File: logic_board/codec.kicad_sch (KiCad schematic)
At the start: 27 parts, among them J1 SJ3-35083C-TR, J4 Conn_01x02, U2 WM8904CGEFL/V, U6 TLV9061xDBV

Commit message: Fix DRC and ERC violations
Also updated some design rules to be consistent with fab.
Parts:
- CR3: footprint Custom_Footprints:1004DFN_LTF -> 1004DFN_LTF
- D2: footprint Diode_SMD:D_SOD-323F -> Diode_SMD:D_SOD-882
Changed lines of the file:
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@@
 			)
 		)
-		(property "Footprint" "Custom_Footprints:1004DFN_LTF"
-			(at 62.23 157.48 0)
+		(property "Footprint" "1004DFN_LTF"
+			(at 51.308 144.78 0)
 			(effects
 				(font
@@
 		)
 		(property "Datasheet" "SP1004U-ULC-04UTG"
-			(at 62.23 157.48 0)
+			(at 52.07 149.098 0)
 			(effects
 				(font
@@
 			)
 		)
-		(property "Footprint" "Diode_SMD:D_SOD-323F"
+		(property "Footprint" "Diode_SMD:D_SOD-882"
 			(at 57.15 106.68 0)
 			(effects
@@
 			)
 		)
-		(property "Datasheet" "https://jlcpcb.com/partdetail/BORN-PESD5V0L1BAN/C920305"
+		(property "Datasheet" "https://assets.nexperia.com/documents/data-sheet/PESD5V0L1UL.pdf"
 			(at 67.31 106.68 0)
 			(effects
@@
 			)
 		)
-		(property "Description" "Low capacitance unidirectional ESD protection diode, 5V, SOD-323"
+		(property "Description" "Low capacitance unidirectional ESD protection diode, 5V, SOD-882"
 			(at 69.85 106.68 0)
 			(effects

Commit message: All signals now routed.
A bit rough, needs some cleanup.
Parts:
- added C31: 0.1uF, Capacitor_SMD:C_0603_1608Metric, symbol Device:C
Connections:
- net +3V3: now also C31.1
- net GND: now also C31.2
- net at C14.2: now also U2.25 (IN1R/DMICDAT2); no longer U2.24 (IN2R)
- net at C15.2: now also U2.26 (IN2L); no longer U2.25 (IN1R/DMICDAT2)
- net at C11.2: now also U2.24 (IN2R); no longer U2.26 (IN2L)

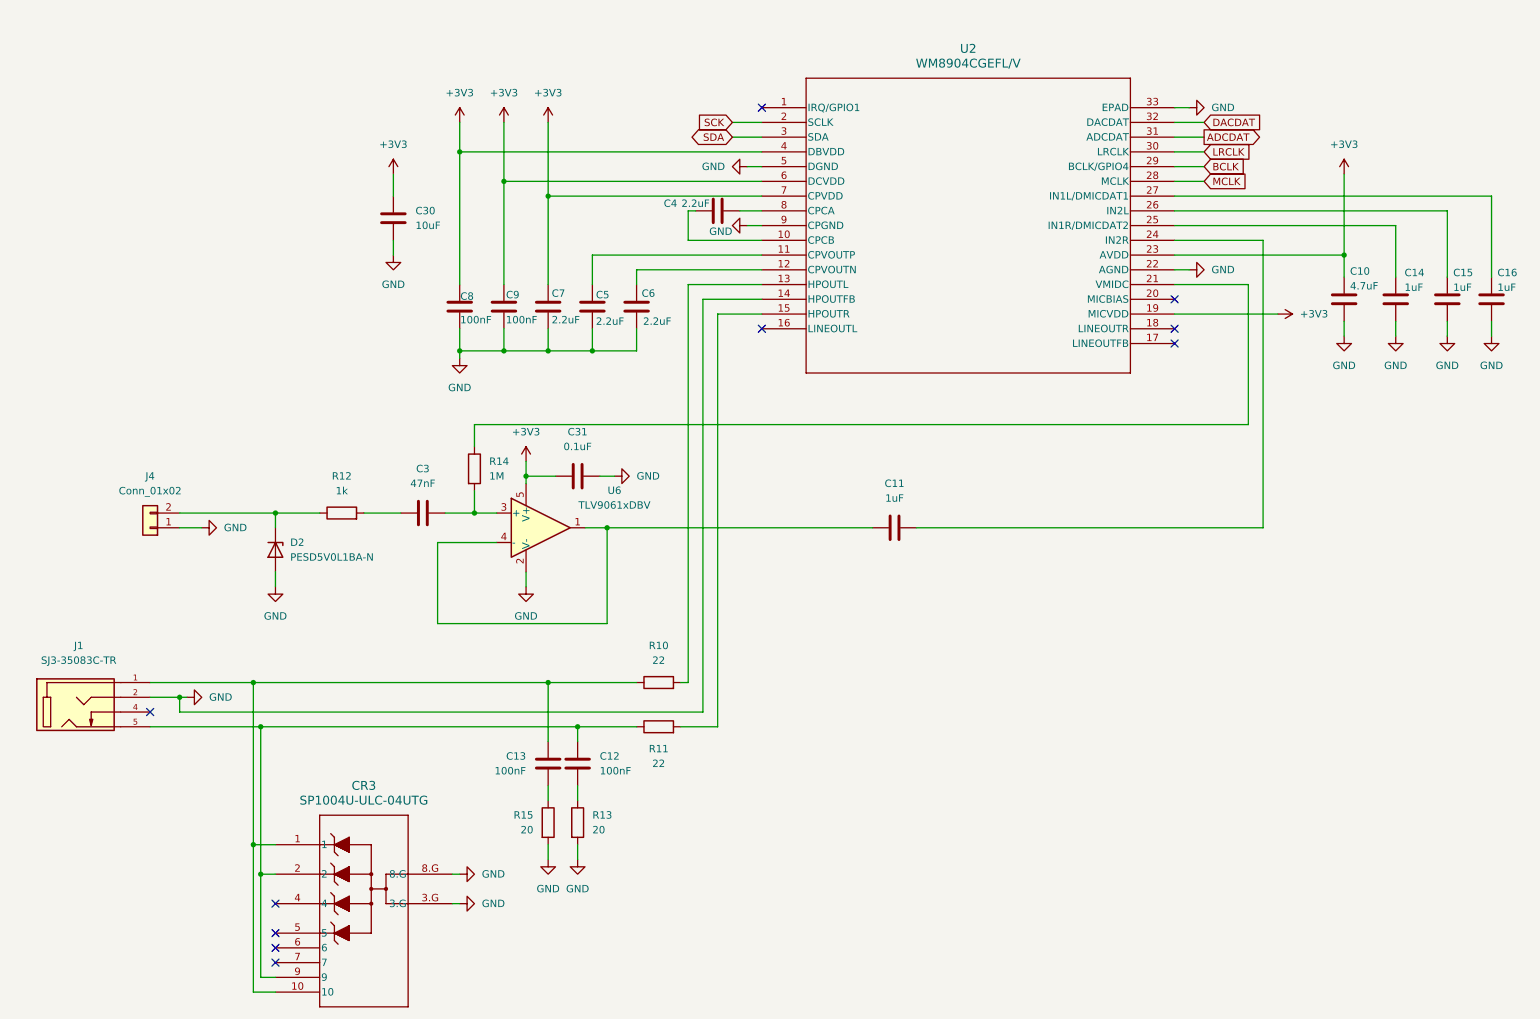
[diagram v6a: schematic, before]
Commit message: Replace WM8904 codec with ES8388
The latter is simpler. Specifically, it doesn't require a 1.8v supply (which I had neglected to hook up). It also doesn't require a ground feedback line from the headphone outputs. It also has a beefier output stage (40mW headphone output vs. 28 @ 30 ohms for the old one)
Also changed the interface from I2S to SPI, avoiding the need for pullup resistors (also missing from previous iteration).
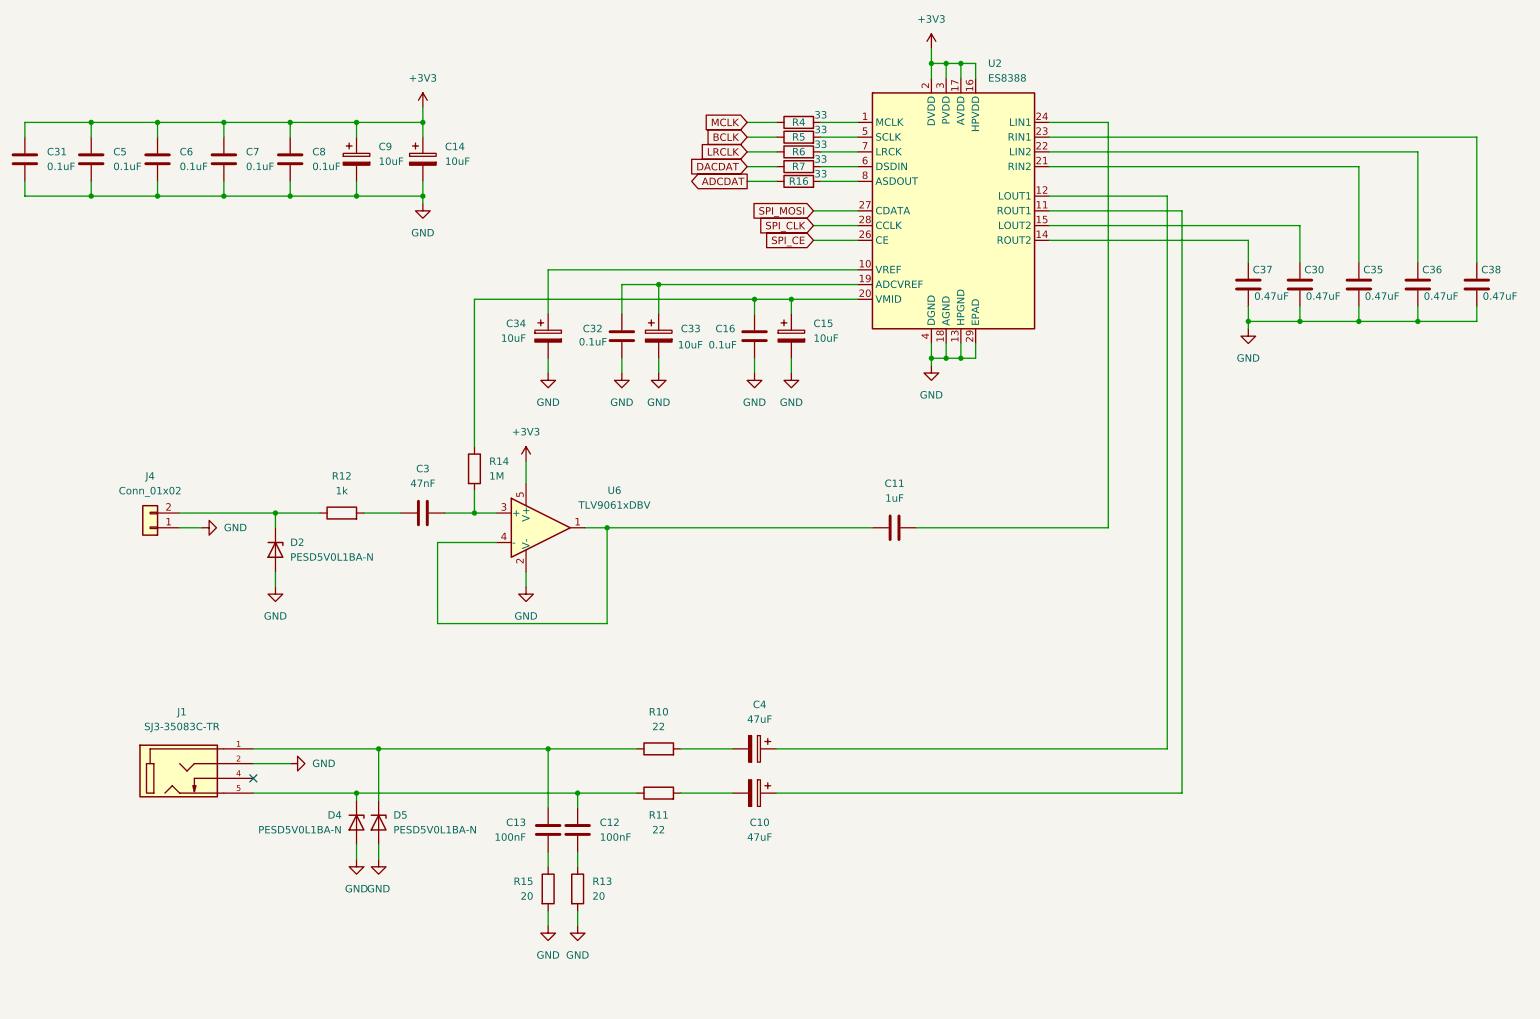
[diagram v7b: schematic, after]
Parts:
- removed C10: 4.7uF, Capacitor_SMD:C_0603_1608Metric, symbol Device:C
- removed C14, C15: 1uF, Capacitor_SMD:C_0603_1608Metric, symbol Device:C
- removed C4: 2.2uF, Capacitor_SMD:C_0603_1608Metric, symbol Device:C
- removed C9: 100nF, Capacitor_SMD:C_0603_1608Metric, symbol Device:C
- removed CR3: SP1004U-ULC-04UTG, 1004DFN_LTF, symbol Custom_Symbols:SP1004U-ULC-04UTG
- removed U2: WM8904CGEFL/V, Custom_Footprints:QFN32_4X4_CIR, symbol Custom_Symbols:WM8904CGEFL_V
- added C10, C4: 47uF, Capacitor_SMD:C_1206_3216Metric, symbol Device:C_Polarized
- added C14, C15, C33, C34, C9: 10uF, Capacitor_SMD:C_0805_2012Metric, symbol Device:C_Polarized
- added C32: 0.1uF, Capacitor_SMD:C_0603_1608Metric, symbol Device:C
- added C35, C36, C37, C38: 0.47uF, Capacitor_SMD:C_0603_1608Metric, symbol Device:C
- added D4, D5: PESD5V0L1BA-N, Diode_SMD:D_SOD-882, symbol Diode:PESD5V0L1UL
- added R16, R4, R5, R6, R7: 33, Resistor_SMD:R_0603_1608Metric, symbol Device:R
- added U2: ES8388, Package_DFN_QFN:QFN-28-1EP_4x4mm_P0.45mm_EP2.6x2.6mm, symbol Audio:ES8388
- C16: value 1uF -> 0.1uF
- C30: value 10uF -> 0.47uF
- C5, C6, C7: value 2.2uF -> 0.1uF
- C8: value 100nF -> 0.1uF
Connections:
- net +3V3: now also C5.1, C6.1, C14.1, C9.1, U2.16 (HPVDD), U2.17 (AVDD), U2.2 (DVDD), U2.3 (PVDD); no longer C30.1
- net ADCDAT: now also R16.1
- net BCLK: now also R5.1
- net DACDAT: now also R7.1
- net GND: now also C16.2, C30.1, C14.2, C15.2, C32.2, C33.2, C34.2, C35.1, C36.1, C37.1, C38.1, C9.2, D4.2 (A), D5.2 (A), U2.13 (HPGND), U2.18 (AGND), U2.29 (EPAD), U2.4 (DGND); no longer C16.1, C30.2
- net LRCLK: now also R6.1
- net MCLK: now also R4.1
- net at C13.1, J1.1, R10.1: now also D5.1 (K)
- net at C12.1, J1.5, R11.1: now also D4.1 (K)
- net at R10.2: now also C4.2
- net at R11.2: now also C10.2
- net at R14.1: now also C16.1, C15.1, U2.20 (VMID)
- net at C11.2: now also U2.24 (LIN1)
- new net: C34.1, U2.10 (VREF)
- new net: R4.2, U2.1 (MCLK)
- new net: C32.1, C33.1, U2.19 (ADCVREF)
- new net: C38.2, U2.23 (RIN1)
- new net: C35.2, U2.21 (RIN2)
- new net: C36.2, U2.22 (LIN2)
- new net: C37.2, U2.14 (ROUT2)
- new net: R7.2, U2.6 (DSDIN)
- new net: R6.2, U2.7 (LRCK)
- new net: R16.2, U2.8 (ASDOUT)
- new net: C4.1, U2.12 (LOUT1)
- new net: R5.2, U2.5 (SCLK)
- new net: C10.1, U2.11 (ROUT1)
- new net: C30.2, U2.15 (LOUT2)
- new net SPI_CE: U2.26 (CE)
- new net SPI_CLK: U2.28 (CCLK)
- new net SPI_MOSI: U2.27 (CDATA)
- no-connect marks 10 -> 1
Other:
- moved on the sheet: C12, C13, J1, R10, R11, R13, R15

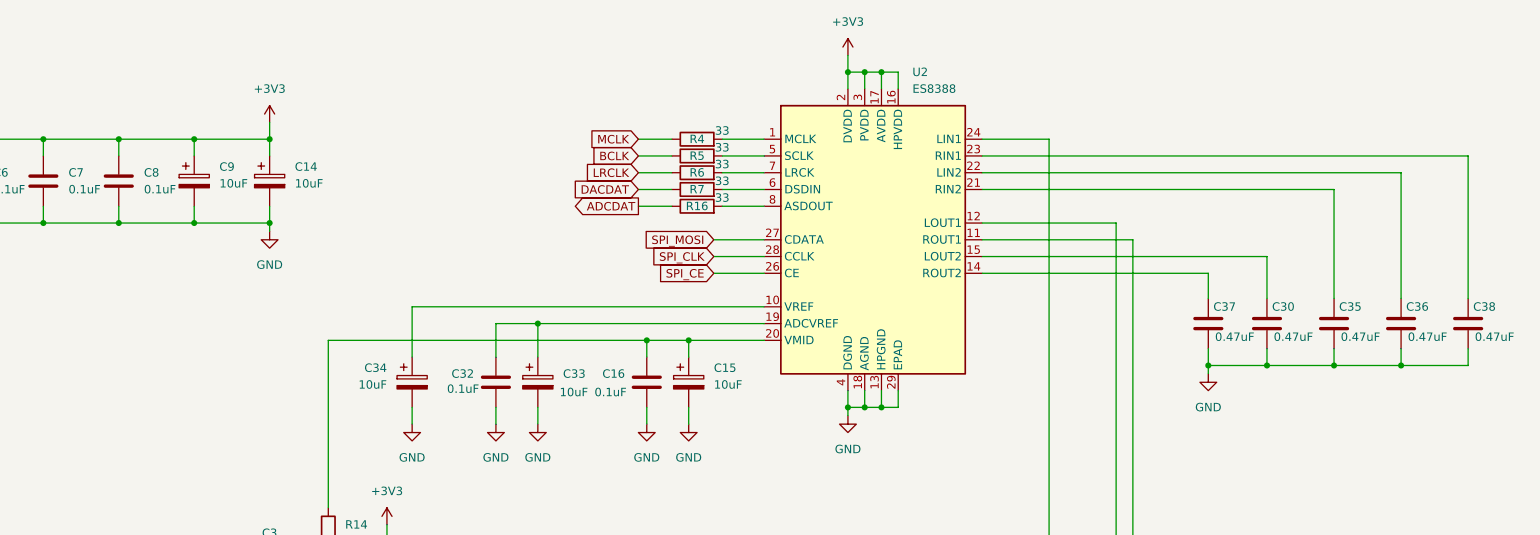
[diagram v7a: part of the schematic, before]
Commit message: Reoriented MCU and moved functions to different pins to try to get them closer to the chips they will connect to to minimize snaking and vias. Laid out bypass caps on codec.
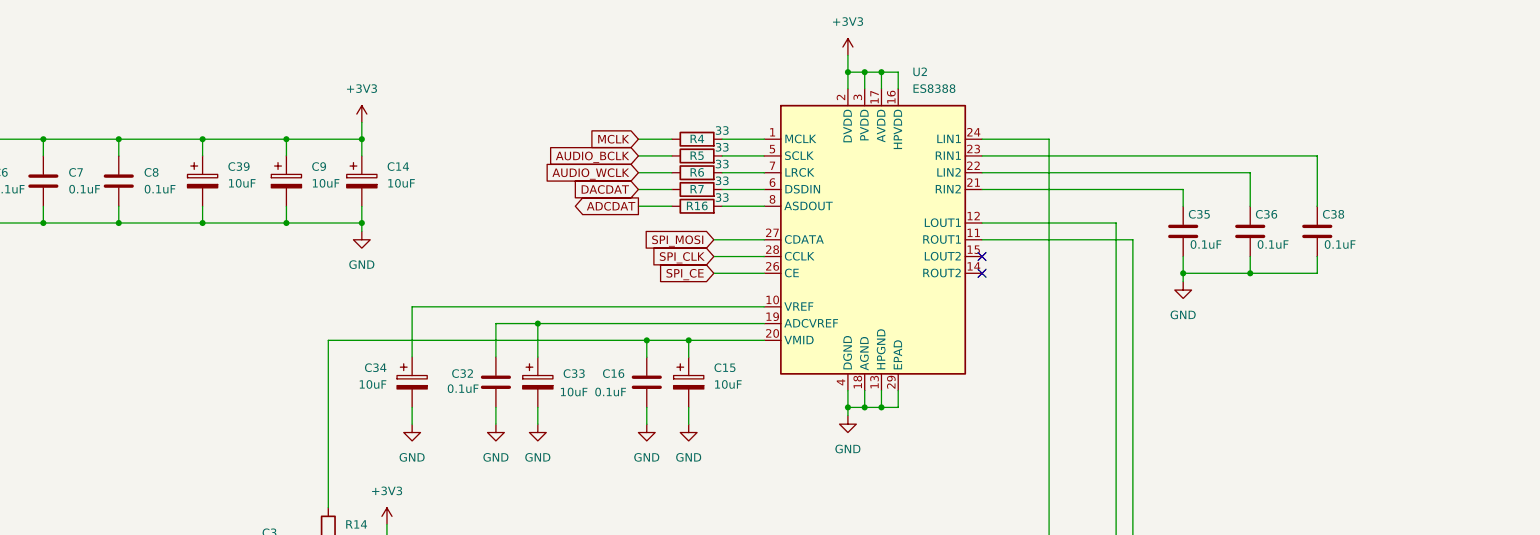
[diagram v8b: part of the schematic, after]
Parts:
- removed C30, C37: 0.47uF, Capacitor_SMD:C_0603_1608Metric, symbol Device:C
- added C39: 10uF, Capacitor_SMD:C_0603_1608Metric, symbol Device:C_Polarized
- C14, C15, C33, C34, C9: footprint Capacitor_SMD:C_0805_2012Metric -> Capacitor_SMD:C_0603_1608Metric
- C16, C31, C32, C5, C6, C7, C8: footprint Capacitor_SMD:C_0603_1608Metric -> Capacitor_SMD:C_0402_1005Metric
- C35, C36, C38: value 0.47uF -> 0.1uF; footprint Capacitor_SMD:C_0603_1608Metric -> Capacitor_SMD:C_0402_1005Metric
- R16, R4, R5, R6, R7: footprint Resistor_SMD:R_0603_1608Metric -> Resistor_SMD:R_0402_1005Metric
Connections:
- net +3V3: now also C39.1
- net GND: now also C39.2
- net BCLK renamed AUDIO_BCLK
- net LRCLK renamed AUDIO_WCLK
- no-connect marks 1 -> 3
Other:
- moved on the sheet: C14, C35, C36, C38, C9
